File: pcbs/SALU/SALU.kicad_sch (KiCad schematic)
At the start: 0 parts

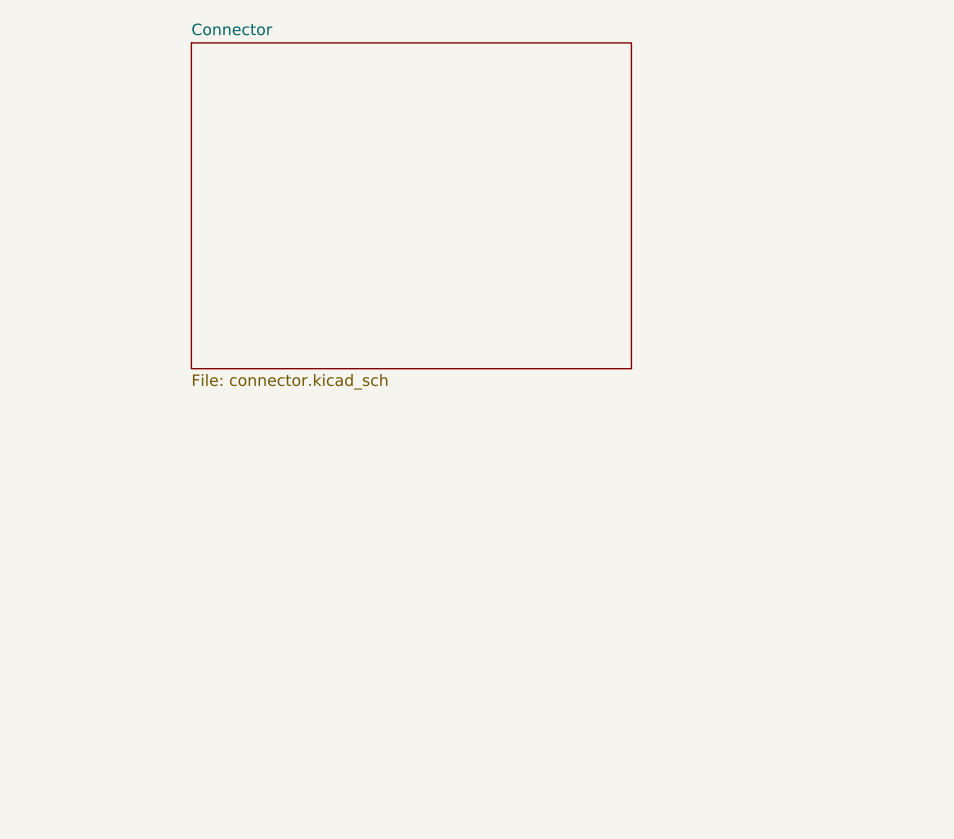
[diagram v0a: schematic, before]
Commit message: Decoder stage
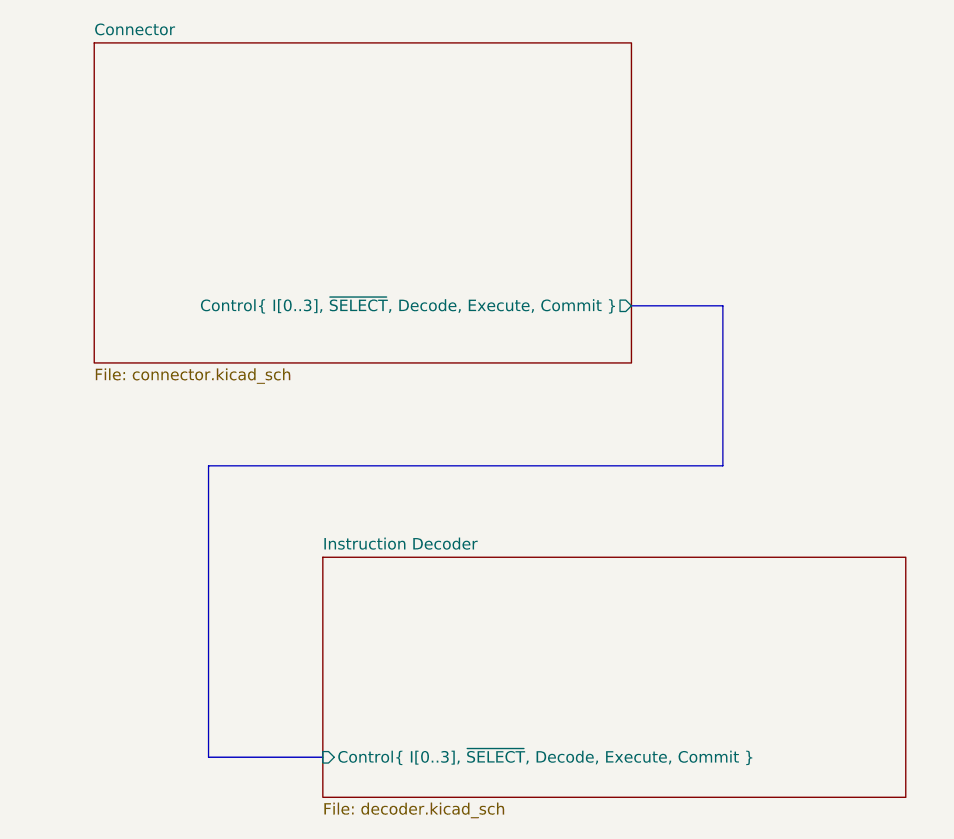
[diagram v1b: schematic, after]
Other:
- added sheet Instruction Decoder (decoder.kicad_sch)
- sheet Connector ports: added Control{ I[0..3], ~{SELECT}, Decode, Execute, Commit }; removed none

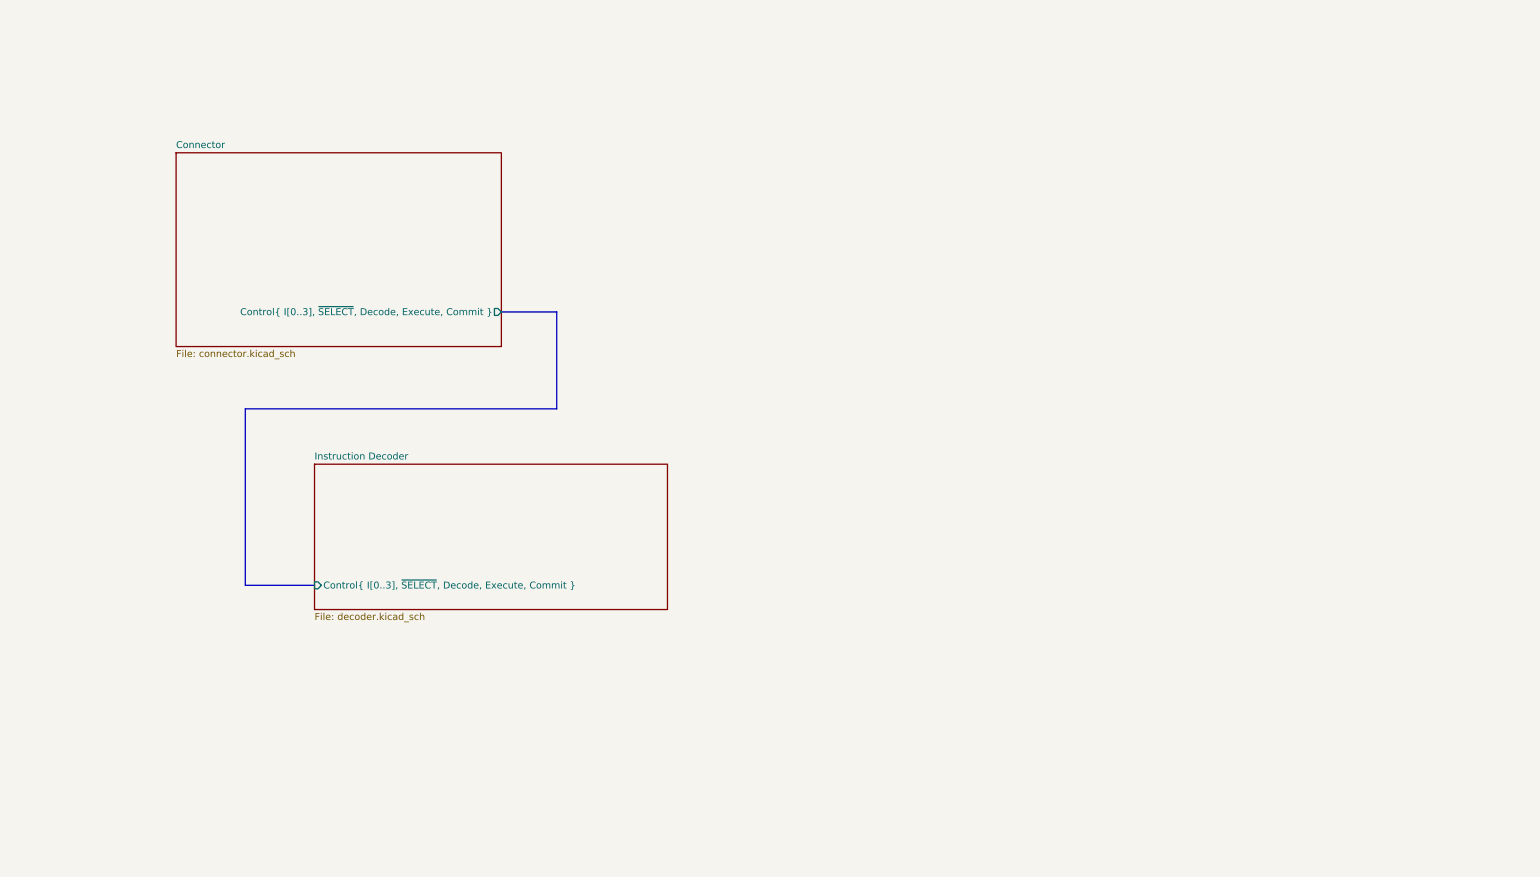
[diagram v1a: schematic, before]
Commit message: Starting on inc/dec
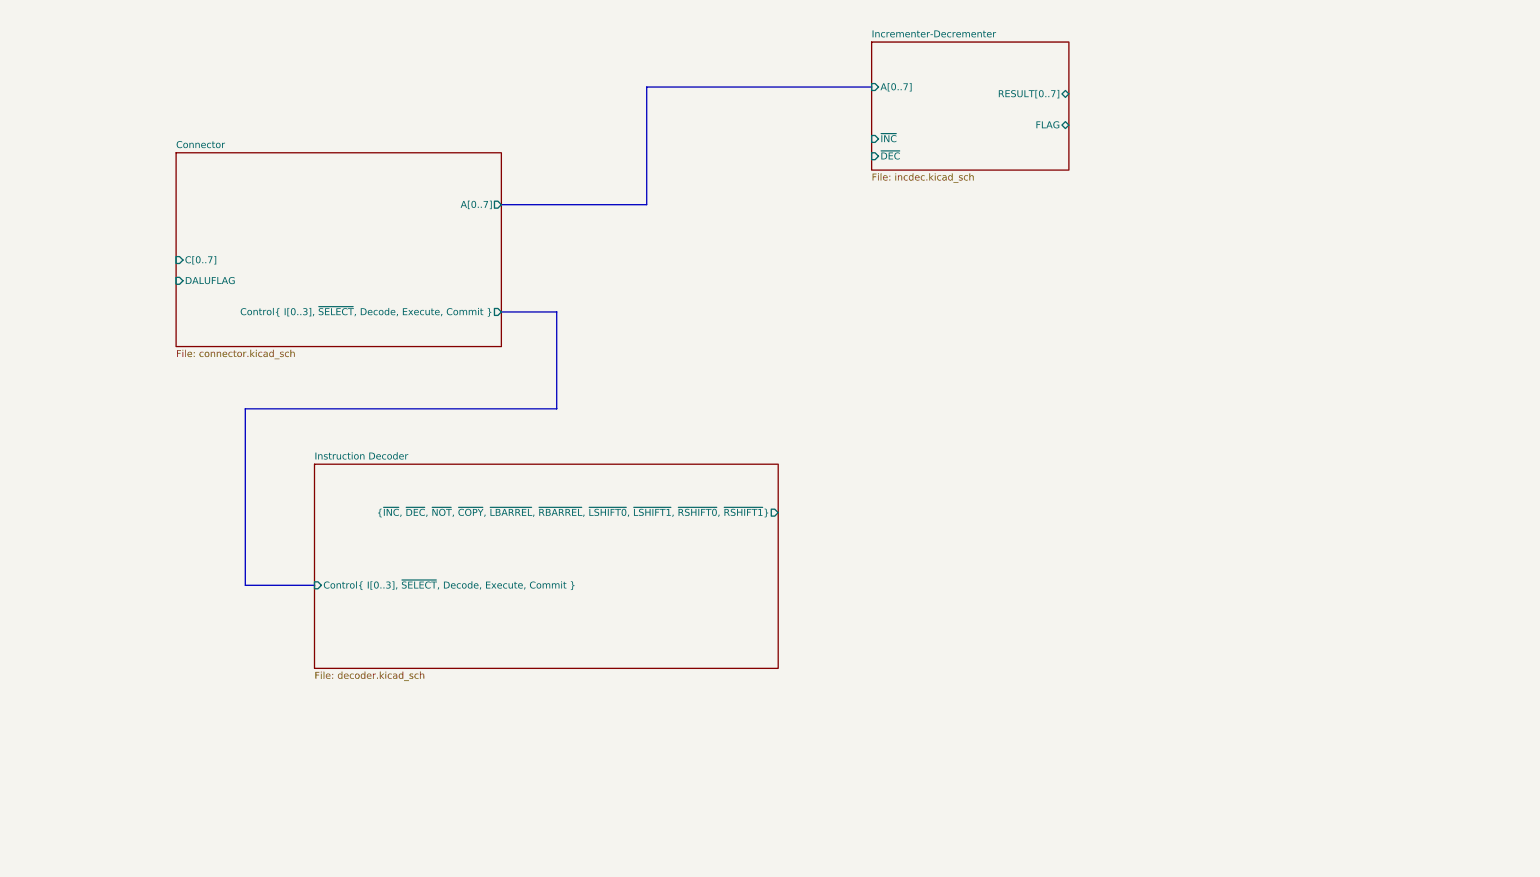
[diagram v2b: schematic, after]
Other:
- added sheet Incrementer-Decrementer (incdec.kicad_sch)
- sheet Connector ports: added A[0..7], C[0..7], DALUFLAG; removed none
- sheet Instruction Decoder ports: added {~{INC}, ~{DEC}, ~{NOT}, ~{COPY}, ~{LBARREL}, ~{RBARREL}, ~{LSHIFT0}, ~{LSHIFT1}, ~{RSHIFT0}, ~{RSHIFT1}}; removed none

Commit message: Some more functions
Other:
- added sheet Barrel Shifters (barrel_shifters.kicad_sch)
- added sheet Not-Copy (not_copy.kicad_sch)

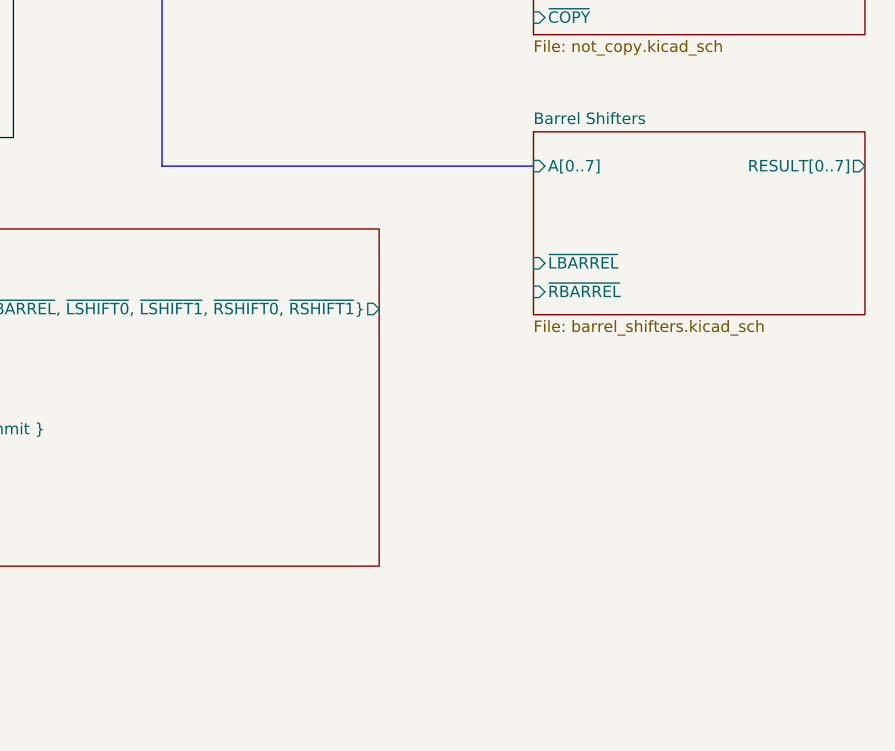
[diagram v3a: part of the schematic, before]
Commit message: Add shifters
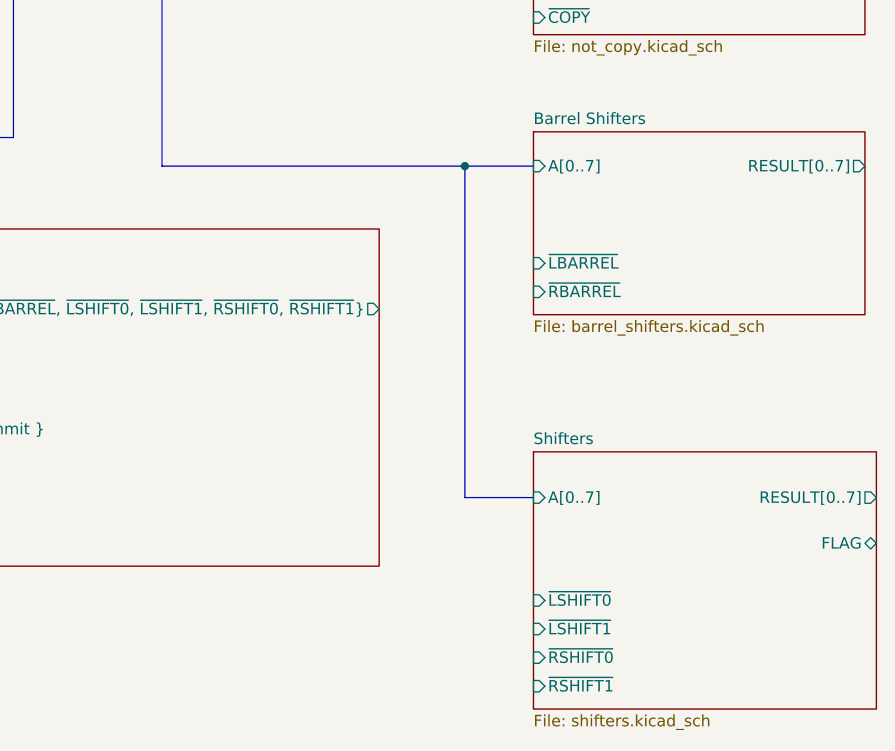
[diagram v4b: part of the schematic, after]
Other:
- added sheet Shifters (shifters.kicad_sch)
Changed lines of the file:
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@@
   (junction (at 107.95 57.785) (diameter 0) (color 0 0 0 0)
   )
+  (junction (at 141.605 90.17) (diameter 0) (color 0 0 0 0)
+  )
   (junction (at 107.95 49.53) (diameter 0) (color 0 0 0 0)
   )
@@
     (stroke (width 0) (type default) (color 0 0 0 0))
   )
+  (bus (pts (xy 149.225 127) (xy 141.605 127))
+    (stroke (width 0) (type default) (color 0 0 0 0))
+  )
   (bus (pts (xy 34.29 86.995) (xy 34.29 119.38))
     (stroke (width 0) (type default) (color 0 0 0 0))
@@
     (stroke (width 0) (type default) (color 0 0 0 0))
   )
-  (bus (pts (xy 149.225 90.17) (xy 107.95 90.17))
+  (bus (pts (xy 149.225 90.17) (xy 141.605 90.17))
     (stroke (width 0) (type default) (color 0 0 0 0))
   )
@@
   )
   (bus (pts (xy 34.29 119.38) (xy 46.99 119.38))
+    (stroke (width 0) (type default) (color 0 0 0 0))
+  )
+  (bus (pts (xy 141.605 90.17) (xy 107.95 90.17))
+    (stroke (width 0) (type default) (color 0 0 0 0))
+  )
+  (bus (pts (xy 141.605 127) (xy 141.605 90.17))
     (stroke (width 0) (type default) (color 0 0 0 0))
   )
@@
     )
     (pin "{~{INC}, ~{DEC}, ~{NOT}, ~{COPY}, ~{LBARREL}, ~{RBARREL}, ~{LSHIFT0}, ~{LSHIFT1}, ~{RSHIFT0}, ~{RSHIFT1}}" output (at 132.08 106.045 0)
+      (effects (font (size 1.27 1.27)) (justify right))
+    )
+  )
+  (sheet (at 149.225 121.92) (size 38.1 28.575) (fields_autoplaced)
+    (stroke (width 0.1524) (type solid) (color 0 0 0 0))
+    (fill (color 0 0 0 0.0000))
+    (property "Sheet name" "Shifters" (id 0) (at 149.225 121.2084 0)
+      (effects (font (size 1.27 1.27)) (justify left bottom))
+    )
+    (property "Sheet file" "shifters.kicad_sch" (id 1) (at 149.225 151.0796 0)
+      (effects (font (size 1.27 1.27)) (justify left top))
+    )
+    (pin "~{LSHIFT0}" input (at 149.225 138.43 180)
+      (effects (font (size 1.27 1.27)) (justify left))
+    )
+    (pin "~{LSHIFT1}" input (at 149.225 141.605 180)
+      (effects (font (size 1.27 1.27)) (justify left))
+    )
+    (pin "A[0..7]" input (at 149.225 127 180)
+      (effects (font (size 1.27 1.27)) (justify left))
+    )
+    (pin "RESULT[0..7]" output (at 187.325 127 0)
+      (effects (font (size 1.27 1.27)) (justify right))
+    )
+    (pin "~{RSHIFT0}" input (at 149.225 144.78 180)
+      (effects (font (size 1.27 1.27)) (justify left))
+    )
+    (pin "~{RSHIFT1}" input (at 149.225 147.955 180)
+      (effects (font (size 1.27 1.27)) (justify left))
+    )
+    (pin "FLAG" tri_state (at 187.325 132.08 0)
       (effects (font (size 1.27 1.27)) (justify right))
     )
@@
     (path "/27468dc9-2b58-4630-b406-58f63eb0bd3b" (page "5"))
     (path "/5e72c66d-a842-4ffb-941e-760d0ca90309" (page "6"))
+    (path "/9d8c817d-a20a-4758-ba85-73c853a6b803" (page "7"))
   )
   (symbol_instances
@@
       (reference "#PWR0608") (unit 1) (value "GND") (footprint "")
     )
+    (path "/9d8c817d-a20a-4758-ba85-73c853a6b803/ec0196c1-5806-4a7f-9390-ee7fc834660a"
+      (reference "#PWR0701") (unit 1) (value "GND") (footprint "")
+    )
+    (path "/9d8c817d-a20a-4758-ba85-73c853a6b803/340618d5-8896-4f98-965c-a6dab486f2f0"
+      (reference "#PWR0702") (unit 1) (value "+5V") (footprint "")
+    )
+    (path "/9d8c817d-a20a-4758-ba85-73c853a6b803/dea2ac99-bfbe-4cc1-9778-effda294c472"
+      (reference "#PWR0703") (unit 1) (value "GND") (footprint "")
+    )
+    (path "/9d8c817d-a20a-4758-ba85-73c853a6b803/2b9967d1-b46f-45e8-ba26-fbc97d7bf8ca"
+      (reference "#PWR0704") (unit 1) (value "+5V") (footprint "")
+    )
+    (path "/9d8c817d-a20a-4758-ba85-73c853a6b803/f2ec1373-aaf3-4efa-bd22-447df2da347c"
+      (reference "#PWR0705") (unit 1) (value "GND") (footprint "")
+    )
+    (path "/9d8c817d-a20a-4758-ba85-73c853a6b803/2d9b91a6-5b5e-499a-acf2-d9dd050eafee"
+      (reference "#PWR0706") (unit 1) (value "+5V") (footprint "")
+    )
+    (path "/9d8c817d-a20a-4758-ba85-73c853a6b803/042e3a32-077a-4375-bdeb-ce55b38a4116"
+      (reference "#PWR0707") (unit 1) (value "GND") (footprint "")
+    )
+    (path "/9d8c817d-a20a-4758-ba85-73c853a6b803/df1b997d-fdec-473a-828c-8de9137f942a"
+      (reference "#PWR0708") (unit 1) (value "+5V") (footprint "")
+    )
+    (path "/9d8c817d-a20a-4758-ba85-73c853a6b803/11ea1e75-b8bf-4025-b000-80df4c29ef51"
+      (reference "#PWR0709") (unit 1) (value "+5V") (footprint "")
+    )
+    (path "/9d8c817d-a20a-4758-ba85-73c853a6b803/ab020599-3625-46ed-9cfb-566b309f233f"
+      (reference "#PWR0710") (unit 1) (value "+5V") (footprint "")
+    )
+    (path "/9d8c817d-a20a-4758-ba85-73c853a6b803/4113700c-8194-46db-8a8a-b631faa40b88"
+      (reference "#PWR0711") (unit 1) (value "GND") (footprint "")
+    )
+    (path "/9d8c817d-a20a-4758-ba85-73c853a6b803/9c0a3cf5-f896-4300-a955-d7ded8e352fa"
+      (reference "#PWR0712") (unit 1) (value "+5V") (footprint "")
+    )
+    (path "/9d8c817d-a20a-4758-ba85-73c853a6b803/280744d7-09f7-4992-b4ee-5177b80bec46"
+      (reference "#PWR0713") (unit 1) (value "GND") (footprint "")
+    )
     (path "/2eb93ddc-e7a7-4cf1-ba9b-2559e5c37953/d90415d0-2507-47f7-a77b-acc1c8b59146"
       (reference "C201") (unit 1) (value "100n") (footprint "Capacitor_SMD:C_0603_1608Metric")
@@
       (reference "C602") (unit 1) (value "100n") (footprint "Capacitor_SMD:C_0603_1608Metric")
     )
+    (path "/9d8c817d-a20a-4758-ba85-73c853a6b803/4baa50ef-3f41-4d58-8fc0-994cf29345db"
+      (reference "C701") (unit 1) (value "100n") (footprint "Capacitor_SMD:C_0603_1608Metric")
+    )
+    (path "/9d8c817d-a20a-4758-ba85-73c853a6b803/13628fe9-df3c-4946-8444-8be3bdbdca8b"
+      (reference "C702") (unit 1) (value "100n") (footprint "Capacitor_SMD:C_0603_1608Metric")
+    )
+    (path "/9d8c817d-a20a-4758-ba85-73c853a6b803/da0372c3-d721-4154-bd91-bd6ec3829b91"
+      (reference "C703") (unit 1) (value "100n") (footprint "Capacitor_SMD:C_0603_1608Metric")
+    )
+    (path "/9d8c817d-a20a-4758-ba85-73c853a6b803/0b003e0c-5dc6-4ea2-b695-0f08d6591c0a"
+      (reference "C704") (unit 1) (value "100n") (footprint "Capacitor_SMD:C_0603_1608Metric")
+    )
     (path "/8ff9c7f7-723f-421c-b21d-a9beb8766b95/d32c1ac6-dfe9-4813-8b89-ff596a3bcf89"
       (reference "D301") (unit 1) (value "GREEN") (footprint "LED_SMD:LED_0603_1608Metric")
@@
       (reference "U602") (unit 1) (value "74HC245") (footprint "Package_SO:SOIC-20W_7.5x12.8mm_P1.27mm")
     )
-  )
+    (path "/9d8c817d-a20a-4758-ba85-73c853a6b803/62bc5b1f-963e-4b51-a099-93d00d8dcb77"
+      (reference "U701") (unit 1) (value "74HC08") (footprint "Package_SO:SOIC-14_3.9x8.7mm_P1.27mm")
+    )
+    (path "/9d8c817d-a20a-4758-ba85-73c853a6b803/2dc83fc2-8175-4535-87bb-85114149a515"
+      (reference "U701") (unit 2) (value "74HC08") (footprint "Package_SO:SOIC-14_3.9x8.7mm_P1.27mm")
+    )
+    (path "/9d8c817d-a20a-4758-ba85-73c853a6b803/e167be17-9a09-4654-a86d-91baf6b41a04"
+      (reference "U701") (unit 3) (value "74HC08") (footprint "Package_SO:SOIC-14_3.9x8.7mm_P1.27mm")
+    )
+    (path "/9d8c817d-a20a-4758-ba85-73c853a6b803/c64f8c39-3a56-4d20-b6d0-c230149a53e3"
+      (reference "U701") (unit 4) (value "74HC08") (footprint "Package_SO:SOIC-14_3.9x8.7mm_P1.27mm")
+    )
+    (path "/9d8c817d-a20a-4758-ba85-73c853a6b803/c5b69fec-e0ce-474f-b278-a0ed84026c13"
+      (reference "U701") (unit 5) (value "74HC08") (footprint "Package_SO:SOIC-14_3.9x8.7mm_P1.27mm")
+    )
+    (path "/9d8c817d-a20a-4758-ba85-73c853a6b803/07a683f4-f921-42de-b5b9-5c7871b84068"
+      (reference "U702") (unit 1) (value "74HCT125") (footprint "Package_DIP:DIP-14_W7.62mm_Socket")
+    )
+    (path "/9d8c817d-a20a-4758-ba85-73c853a6b803/42577b10-5362-45d6-9c0b-861ec8a8c0f4"
+      (reference "U702") (unit 2) (value "74HCT125") (footprint "Package_DIP:DIP-14_W7.62mm_Socket")
+    )
+    (path "/9d8c817d-a20a-4758-ba85-73c853a6b803/b33b038c-0144-47fa-a793-a19cd076ddce"
+      (reference "U702") (unit 3) (value "74HCT125") (footprint "Package_DIP:DIP-14_W7.62mm_Socket")
+    )
+    (path "/9d8c817d-a20a-4758-ba85-73c853a6b803/c994c432-80fe-4b64-ab56-a613f9c2dc6d"
+      (reference "U702") (unit 4) (value "74HCT125") (footprint "Package_DIP:DIP-14_W7.62mm_Socket")
+    )
+    (path "/9d8c817d-a20a-4758-ba85-73c853a6b803/9f44ee6b-f7e1-4988-b90b-9507389e41ab"
+      (reference "U702") (unit 5) (value "74HCT125") (footprint "Package_DIP:DIP-14_W7.62mm_Socket")
+    )
+    (path "/9d8c817d-a20a-4758-ba85-73c853a6b803/4ee7d4c3-babf-404f-bce3-cbc6fbb517c2"
+      (reference "U703") (unit 1) (value "74HC245") (footprint "Package_SO:SOIC-20W_7.5x12.8mm_P1.27mm")
+    )
+    (path "/9d8c817d-a20a-4758-ba85-73c853a6b803/2aca1938-65ea-4e4b-9638-a60fe488dff6"
+      (reference "U704") (unit 1) (value "74HC245") (footprint "Package_SO:SOIC-20W_7.5x12.8mm_P1.27mm")
+    )
+  )

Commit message: Routing, routing, routing
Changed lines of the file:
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@@
+    (stroke (width 0) (type default) (color 0 0 0 0))
+  )
+  (bus (pts (xy 197.485 58.42) (xy 186.055 58.42))
     (stroke (width 0) (type default) (color 0 0 0 0))
   )
@@
     (stroke (width 0) (type default) (color 0 0 0 0))
   )
+  (bus (pts (xy 197.485 29.21) (xy 197.485 58.42))
+    (stroke (width 0) (type default) (color 0 0 0 0))
+  )
   (bus (pts (xy 141.605 127) (xy 141.605 90.17))
+    (stroke (width 0) (type default) (color 0 0 0 0))
+  )
+  (bus (pts (xy 185.42 29.21) (xy 197.485 29.21))
     (stroke (width 0) (type default) (color 0 0 0 0))
   )
@@
       (effects (font (size 1.27 1.27)) (justify left))
     )
-    (pin "RESULT[0..7]" output (at 186.055 57.785 0)
+    (pin "RESULT[0..7]" tri_state (at 186.055 58.42 0)
       (effects (font (size 1.27 1.27)) (justify right))
     )
